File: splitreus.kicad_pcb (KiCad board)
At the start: 2 copper layers, 132.5 x 101 mm, 71 parts, among them J1 TRRS, SW0 SW_PUSH, SW1 SW_PUSH, SW10 SW_PUSH, SW11 SW_PUSH, SW12 SW_PUSH, SW13 SW_PUSH, SW14 SW_PUSH, SW15 SW_PUSH, SW16 SW_PUSH, SW17 SW_PUSH, SW18 SW_PUSH, SW19 SW_PUSH, SW2 SW_PUSH, SW20 SW_PUSH, SW21 SW_PUSH, SW22 SW_PUSH, SW23 SW_PUSH, SW24 SW_PUSH, SW25 SW_PUSH, SW26 SW_PUSH, SW27 SW_PUSH, SW28 SW_PUSH, SW29 SW_PUSH, SW3 SW_PUSH, SW30 SW_PUSH, SW4 SW_PUSH, SW5 SW_PUSH, SW6 SW_PUSH, SW7 SW_PUSH, SW8 SW_PUSH, SW9 SW_PUSH, U1 ProMicro

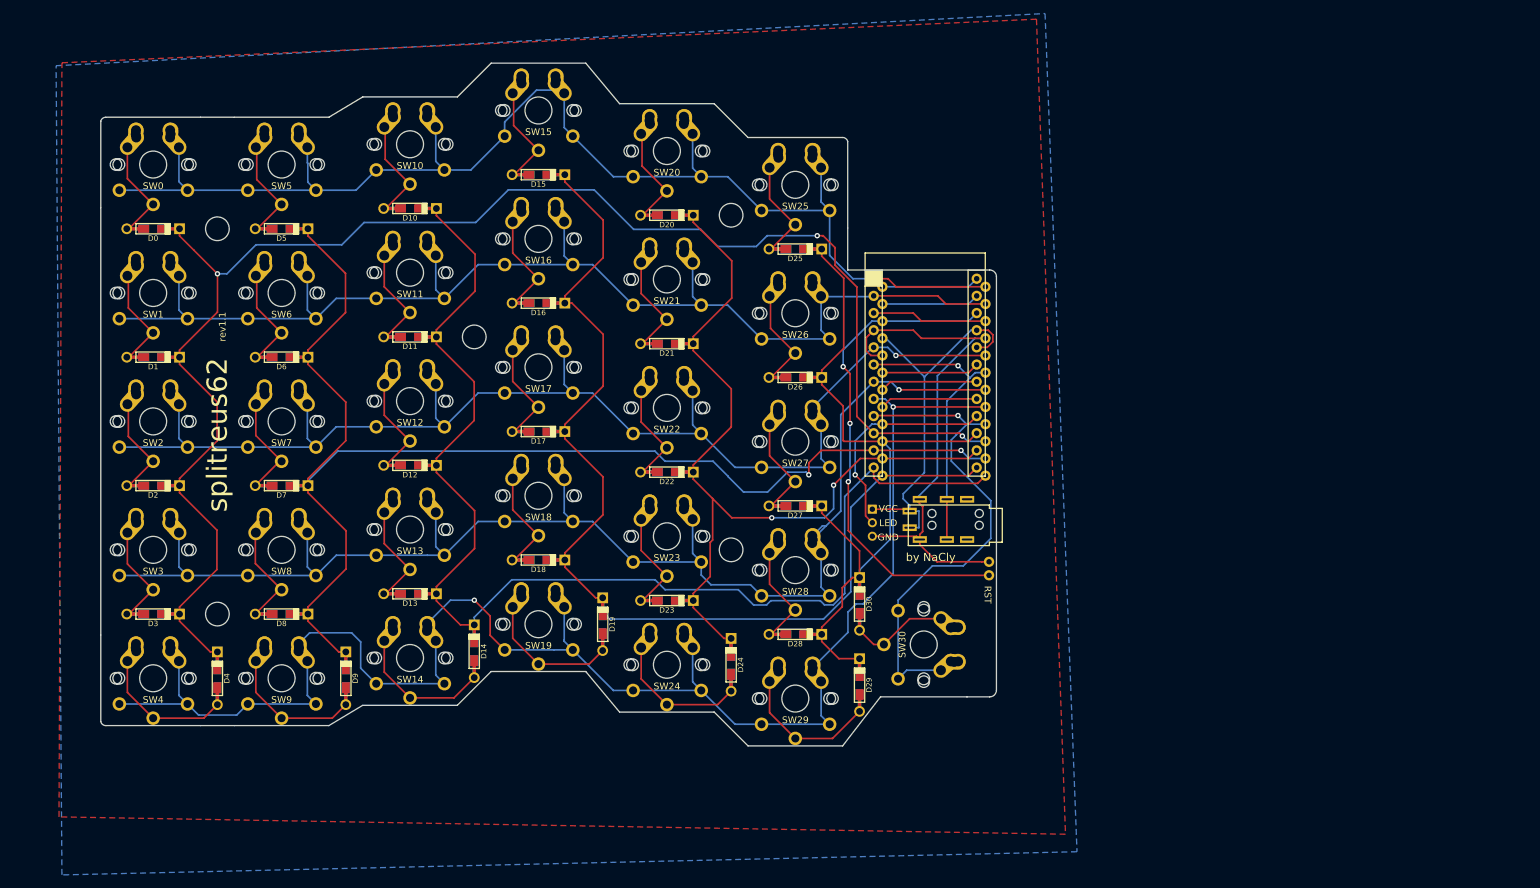
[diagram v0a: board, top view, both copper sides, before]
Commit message: Created kailh_hot_swap
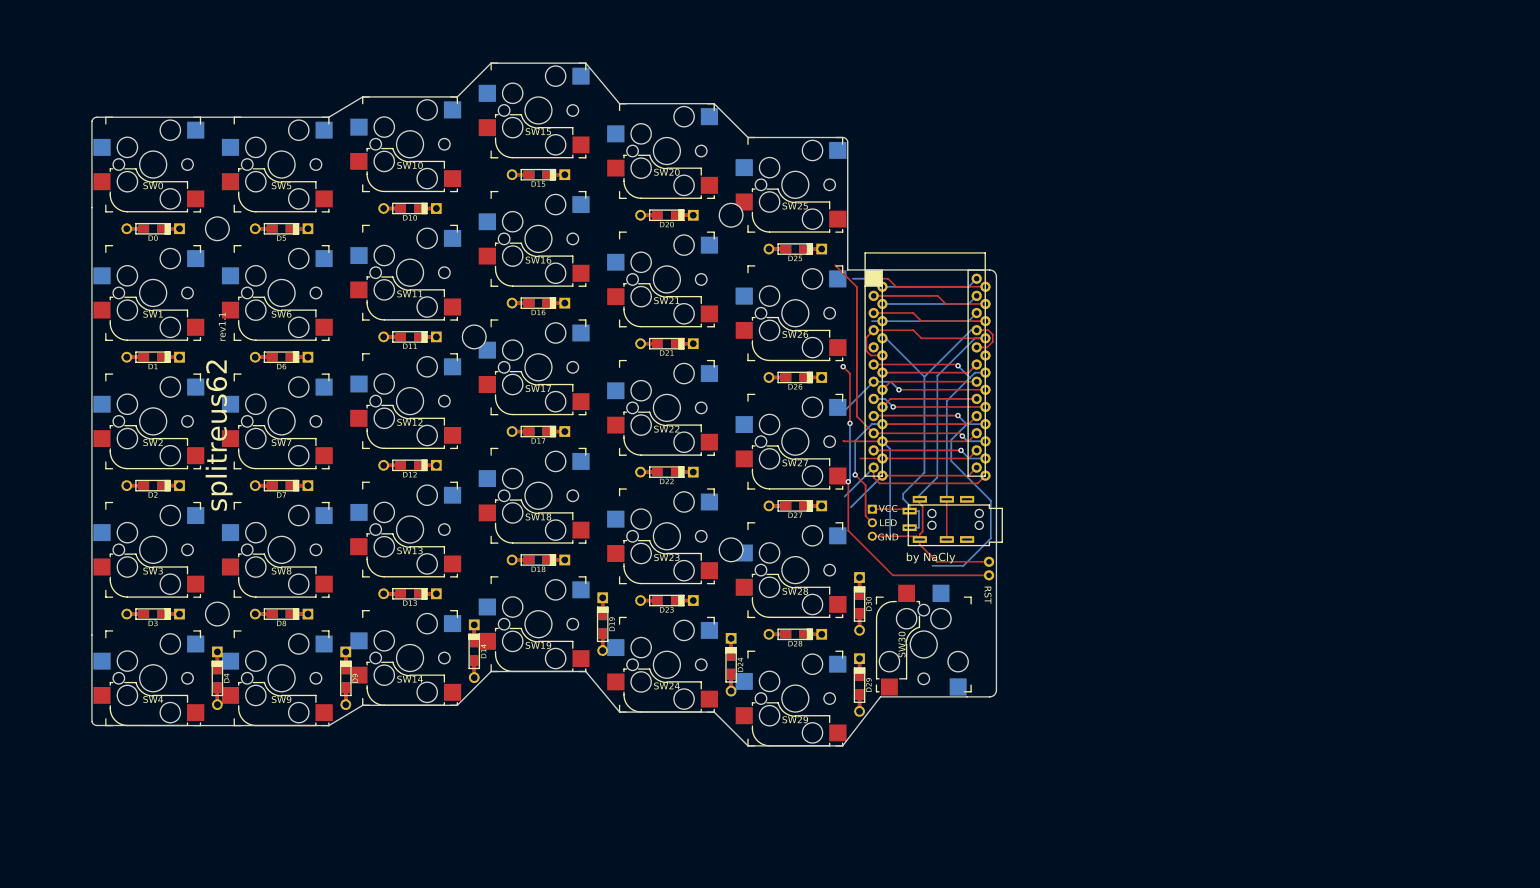
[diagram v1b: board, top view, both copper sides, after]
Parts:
- SW0, SW1, SW10, SW11, SW12, SW13, SW14, SW15, SW16, SW17, SW18, SW19, SW2, SW20, SW21, SW22, SW23, SW24, SW25, SW26, SW27, SW28, SW29, SW3, SW30, SW4, SW5, SW6, SW7, SW8, SW9: footprint Custom Footies:MX-Alps-Choc-1U-No-reversible-fixed -> daprice_kail_mx:Kailh_socket_MX_reversible
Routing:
- net ROW4: track 255.4 -> 17.0 mm, vias 2 -> 1
- net ROW2: track 206.6 -> 0.00 mm, vias 1 -> 0
- net ROW3: track 224.1 -> 23.9 mm
- net COL0: track 240.1 -> 44.3 mm, vias 3 -> 1
- net ROW0: track 209.9 -> 20.1 mm
- net COL1: track 201.9 -> 17.0 mm, vias 2 -> 1
- net ROW1: track 201.7 -> 17.2 mm
- net COL2: track 191.9 -> 24.9 mm
- net COL3: track 165.1 -> 21.1 mm
- net COL4: track 136.2 -> 17.7 mm, vias 2 -> 0
- net COL5: track 122.1 -> 37.8 mm
- net Net-(D29-Pad1): track 26.8 -> 0.00 mm
- net Net-(D14-Pad1): track 26.4 -> 0.00 mm
- net Net-(D9-Pad1): track 26.0 -> 0.00 mm
- net Net-(D4-Pad1): track 26.0 -> 0.00 mm
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- removed copper zone on B.Cu, net (none)
- removed copper zone on F.Cu, net (none)
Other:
- board size 132.5 x 101 mm -> 133.8 x 101 mm

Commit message: updated files
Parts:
- removed REF** (x4): MountingHole_3.5mm, MountingHole:MountingHole_3.5mm
- RST1: footprint Connector_PinHeader_1.27mm:PinHeader_1x02_P1.27mm_Vertical -> Lily58-footprint:TACT_SWITCH_TVBP06
- moved RST1 1.14 mm to (122.6, 61.2), turned to 90 degrees
- renumbered REF** to HOLE4
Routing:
- net RST: track 64.3 -> 14.4 mm, vias 3 -> 0
- net ROW5: track 47.7 -> 17.1 mm
- net COL0: track 44.3 -> 17.0 mm
- net ROW3: track 23.9 -> 17.0 mm
- net COL3: track 21.1 -> 14.4 mm
- net COL2: track 24.9 -> 18.8 mm
- net COL5: track 37.8 -> 31.9 mm
- net COL4: track 17.7 -> 14.4 mm
- net ROW0: track 20.1 -> 17.0 mm
- net GND: track 78.6 -> 76.8 mm

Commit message: Update
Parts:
- removed HOLE4: MountingHole_3.5mm, MountingHole:MountingHole_3.5mm
- moved RST1 8.44 mm to (114.6, 58.7), turned to 0 degrees
- moved D19 0.65 mm to (65.8, 68.0)
- moved D24 0.65 mm to (84.8, 74.0)
- moved D4 0.65 mm to (8.85, 76.0)
- moved D14 0.65 mm to (46.9, 72.0)
- moved D9 0.65 mm to (27.9, 76.0)
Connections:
- U1 pad 20: VCC -> GND
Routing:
- net ROW4: track 17.0 -> 314.6 mm, vias 1 -> 2
- net ROW1: track 17.2 -> 297.6 mm, vias 0 -> 1
- net ROW3: track 17.0 -> 280.4 mm, vias 1 -> 4
- net ROW2: track 0.00 -> 246.4 mm, vias 0 -> 3
- net ROW0: track 17.0 -> 256.8 mm, vias 0 -> 2
- net COL0: track 17.0 -> 239.3 mm
- net COL1: track 17.0 -> 221.3 mm
- net COL2: track 18.8 -> 194.5 mm
- net COL3: track 14.4 -> 171.3 mm, vias 0 -> 1
- net COL4: track 14.4 -> 140.0 mm, vias 0 -> 1
- net COL5: track 31.9 -> 131.2 mm
- net ROW5: track 17.1 -> 81.6 mm
- net RST: track 14.4 -> 62.0 mm
- net Net-(D15-Pad1): track 0.00 -> 46.4 mm
- net Net-(D6-Pad1): track 0.00 -> 39.6 mm
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- added copper zone on B.Cu, net (none)
- added copper zone on F.Cu, net (none)
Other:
- board text added: "rev2.0"
- board text removed: "rev1.1"

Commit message: Update
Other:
- board text removed: "RST"
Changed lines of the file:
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@@
   (general
     (thickness 1.6)
-    (drawings 456)
+    (drawings 454)
     (tracks 1298)
     (zones 0)
@@
   )
   (layers
-    (0 F.Cu signal)
-    (31 B.Cu signal)
+    (0 F.Cu signal hide)
+    (31 B.Cu signal hide)
     (32 B.Adhes user)
     (33 F.Adhes user hide)
@@
       (drillshape 0)
       (scaleselection 1)
-      (outputdirectory "gerber/"))
+      (outputdirectory "C:/Users/Derek/Documents/gerber/sp62_hot/"))
   )
   (net 0 "")
@@
     )
   )
-  (gr_text RST (at 123.4608 63.6372 270) (layer B.SilkS)
-    (effects (font (size 1 1) (thickness 0.2)) (justify mirror))
-  )
-  (gr_text RST (at 123.4608 63.6372 270) (layer F.SilkS)
-    (effects (font (size 1 1) (thickness 0.2)))
-  )
   (gr_text "by NaCly" (at 123.6386 60.7924 270) (layer F.SilkS)
     (effects (font (size 1.2 1.2) (thickness 0.2)))
@@
   (segment (start 105.503 27.5718) (end 105.503 25.597) (width 0.25) (layer F.Cu) (net 40))
   (segment (start 105.503 25.597) (end 106.59 24.51) (width 0.25) (layer F.Cu) (net 40))
+  (segment (start 108.0165 28.1181) (end 108.0164 28.1181) (width 0.25) (layer B.Cu) (net 40))
+  (segment (start 108.0164 28.1181) (end 107.8888 28.2457) (width 0.25) (layer B.Cu) (net 40))
+  (segment (start 108.0165 28.1181) (end 107.889 28.2457) (width 0.25) (layer B.Cu) (net 40))
   (segment (start 84.85 70.1) (end 83.7247 70.1) (width 0.25) (layer F.Cu) (net 41))
   (segment (start 79.9 64.5) (end 79.9 65.6253) (width 0.25) (layer F.Cu) (net 41))
@@
   (segment (start 107.889 20.6257) (end 120.634 20.6257) (width 0.25) (layer B.Cu) (net 45))
   (segment (start 120.634 20.6257) (end 121.83 19.43) (width 0.25) (layer B.Cu) (net 45))
-  (segment (start 108.0165 28.1181) (end 108.0164 28.1181) (width 0.25) (layer B.Cu) (net 40))
-  (segment (start 108.0164 28.1181) (end 107.8888 28.2457) (width 0.25) (layer B.Cu) (net 40))
-  (segment (start 108.0165 28.1181) (end 107.889 28.2457) (width 0.25) (layer B.Cu) (net 40))
   (segment (start 107.889 25.7057) (end 107.8888 25.7057) (width 0.25) (layer B.Cu) (net 46))
   (segment (start 108.144 25.7057) (end 107.889 25.7057) (width 0.25) (layer B.Cu) (net 46))

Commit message: a lot
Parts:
- removed VCC: PinHeader_1x03_P2.00mm_Vertical, Connector_PinHeader_2.00mm:PinHeader_1x03_P2.00mm_Vertical
- D0, D1, D10, D11, D12, D13, D14, D15, D16, D17, D18, D19, D2, D20, D21, D22, D23, D24, D25, D26, D27, D28, D29, D3, D30, D4, D5, D6, D7, D8, D9: value DIODE_SCHOTTKY_SOT23 -> 1N4148; footprint keebio:Diode-Hybrid-reversible -> Custom Footies:Diode-Hybrid-reversible
- U1: footprint Lily58-footprint:ProMicro_rev2 -> Custom Footies:nice_nano
- moved RST1 23.7 mm to (138.2, 59.9)
- moved U1 0.47 mm to (115.4, 32.1), turned to 270 degrees
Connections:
- U1 pad 1: ROW0 -> SERIAL
- U1 pad 10: COL0 -> ROW4
- U1 pad 11: COL1 -> ROW5
- U1 pad 12: COL2 -> COL0
- U1 pad 13: COL3 -> COL1
- U1 pad 14: COL4 -> COL2
- U1 pad 15: COL5 -> COL3
- U1 pad 16: LED -> COL4
- U1 pad 17: Net-(U1-Pad17) -> COL5
- U1 pad 18: Net-(U1-Pad18) -> (no net)
- U1 pad 19: Net-(U1-Pad19) -> (no net)
- U1 pad 2: ROW1 -> ROW0
- U1 pad 20: GND -> VCC
- U1 pad 23: Net-(U1-Pad23) -> GND
- U1 pad 24: Net-(U1-Pad24) -> (no net)
- U1 pad 3: Net-(U1-Pad3) -> GND
- U1 pad 5: ROW2 -> (no net)
- U1 pad 6: SERIAL -> (no net)
- U1 pad 7: ROW3 -> ROW1
- U1 pad 8: ROW4 -> ROW2
- U1 pad 9: ROW5 -> ROW3
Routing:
- net ROW4: track 314.6 -> 0.00 mm, vias 2 -> 0
- net ROW1: track 297.6 -> 0.00 mm, vias 1 -> 0
- net ROW3: track 280.4 -> 0.00 mm, vias 4 -> 0
- net ROW0: track 256.8 -> 0.00 mm, vias 2 -> 0
- net ROW2: track 246.4 -> 0.00 mm, vias 3 -> 0
- net COL0: track 239.3 -> 0.00 mm, vias 1 -> 0
- net COL1: track 221.3 -> 0.00 mm, vias 1 -> 0
- net COL2: track 194.5 -> 0.00 mm
- net COL3: track 171.3 -> 0.00 mm, vias 1 -> 0
- net COL4: track 140.0 -> 0.00 mm, vias 1 -> 0
- net COL5: track 131.2 -> 0.00 mm
- net ROW5: track 81.6 -> 0.00 mm, vias 1 -> 0
- net GND: track 73.4 -> 0.00 mm
- net RST: track 62.0 -> 0.00 mm
- net VCC: track 58.0 -> 0.00 mm
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- removed copper zone on B.Cu, net (none)
- removed copper zone on F.Cu, net (none)
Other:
- board size 133.8 x 101 mm -> 134.3 x 107.2 mm
- board text removed: "by NaCly"
- board text removed: "rev2.0"
- board text removed: "splitreus62"

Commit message: traces
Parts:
- added J2: battery, Connector_PinSocket_2.54mm:PinSocket_1x02_P2.54mm_Vertical, F.Cu at (116.3, 16.0)
- SW0, SW1, SW10, SW11, SW12, SW13, SW14, SW15, SW16, SW17, SW18, SW19, SW2, SW20, SW21, SW22, SW23, SW24, SW25, SW26, SW27, SW28, SW29, SW3, SW30, SW4, SW5, SW6, SW7, SW8, SW9: footprint daprice_kail_mx:Kailh_socket_MX_reversible -> Custom Footies:Kailh_socket_MX_reversible_fix
- moved D29 13.6 mm to (95.2, 87.0), turned to 0 degrees
- moved D14 12.6 mm to (38.1, 81.0), turned to 0 degrees
- moved D4 11.9 mm to (0.00, 84.0), turned to 0 degrees
- moved D9 11.9 mm to (19.1, 84.0), turned to 0 degrees
- moved D19 11.8 mm to (57.1, 76.0), turned to 0 degrees
- moved D24 11.8 mm to (76.2, 82.0), turned to 0 degrees
- moved D30 5.19 mm to (105.9, 70.0), turned to 270 degrees
- moved SW29 0.32 mm to (95.2, 79.2)
- moved SW28 0.29 mm to (95.2, 60.1)
- moved SW24 0.28 mm to (76.2, 74.2)
- moved SW27 0.27 mm to (95.2, 41.1)
- moved SW26 0.25 mm to (95.2, 22.1)
- moved SW19 0.25 mm to (57.1, 68.2)
- moved SW23 0.25 mm to (76.2, 55.1)
- moved D25 0.25 mm to (95.2, 12.5)
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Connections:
- U1 pad 10: ROW4 -> COL2
- U1 pad 11: ROW5 -> ROW2
- U1 pad 12: COL0 -> COL3
- U1 pad 13: COL1 -> ROW3
- U1 pad 14: COL2 -> COL4
- U1 pad 15: COL3 -> ROW4
- U1 pad 16: COL4 -> COL5
- U1 pad 17: COL5 -> ROW5
- U1 pad 2: ROW0 -> COL0
- U1 pad 7: ROW1 -> ROW0
- U1 pad 8: ROW2 -> COL1
- U1 pad 9: ROW3 -> ROW1
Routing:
- net COL0: track 0.00 -> 252.0 mm
- net COL1: track 0.00 -> 210.4 mm, vias 0 -> 2
- net ROW4: track 0.00 -> 173.0 mm, vias 0 -> 7
- net COL2: track 0.00 -> 172.3 mm, vias 0 -> 2
- net ROW0: track 0.00 -> 165.7 mm, vias 0 -> 6
- net ROW3: track 0.00 -> 165.7 mm, vias 0 -> 6
- net COL4: track 0.00 -> 155.1 mm, vias 0 -> 2
- net ROW1: track 0.00 -> 149.9 mm, vias 0 -> 6
- net COL3: track 0.00 -> 148.5 mm, vias 0 -> 2
- net ROW2: track 0.00 -> 130.9 mm, vias 0 -> 6
- net COL5: track 0.00 -> 125.3 mm, vias 0 -> 1
- net ROW5: track 0.00 -> 62.6 mm, vias 0 -> 2
- net GND: track 0.00 -> 50.8 mm
- net SERIAL: track 0.00 -> 42.0 mm
- net VCC: track 0.00 -> 37.0 mm, vias 0 -> 1
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
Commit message: traces routed
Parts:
- moved RST1 42.1 mm to (118.7, 22.7), turned to 90 degrees
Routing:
- net RST: track 0.00 -> 5.70 mm
- net GND: track 50.8 -> 52.1 mm

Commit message: leds
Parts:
- added D90: SK6812MINI, Custom Footies:sk6812_minie_reversible, F.Cu at (163.5, 30.8)
- added D91: SK6812MINI, Custom Footies:sk6812_minie_reversible, F.Cu at (156.4, 15.6)
- added D910: SK6812MINI, Custom Footies:sk6812_minie_reversible, F.Cu at (156.4, 30.8)
- added D911: SK6812MINI, Custom Footies:sk6812_minie_reversible, F.Cu at (163.5, 25.7)
- added D912: SK6812MINI, Custom Footies:sk6812_minie_reversible, F.Cu at (170.5, 20.7)
- added D913: SK6812MINI, Custom Footies:sk6812_minie_reversible, F.Cu at (177.5, 15.6)
- added D914: SK6812MINI, Custom Footies:sk6812_minie_reversible, F.Cu at (184.5, 10.6)
- added D915: SK6812MINI, Custom Footies:sk6812_minie_reversible, F.Cu at (170.5, 25.7)
- added D916: SK6812MINI, Custom Footies:sk6812_minie_reversible, F.Cu at (154.7, 5.84)
- added D917: SK6812MINI, Custom Footies:sk6812_minie_reversible, F.Cu at (177.5, 20.7)
- added D918: SK6812MINI, Custom Footies:sk6812_minie_reversible, F.Cu at (184.5, 15.6)
- added D919: SK6812MINI, Custom Footies:sk6812_minie_reversible, F.Cu at (191.5, 10.6)
- added D92: SK6812MINI, Custom Footies:sk6812_minie_reversible, F.Cu at (163.5, 10.6)
- added D920: SK6812MINI, Custom Footies:sk6812_minie_reversible, F.Cu at (170.5, 30.8)
- added D921: SK6812MINI, Custom Footies:sk6812_minie_reversible, F.Cu at (177.5, 25.7)
- added D922: SK6812MINI, Custom Footies:sk6812_minie_reversible, F.Cu at (184.5, 20.7)
- added D923: SK6812MINI, Custom Footies:sk6812_minie_reversible, F.Cu at (191.5, 15.6)
- added D924: SK6812MINI, Custom Footies:sk6812_minie_reversible, F.Cu at (198.6, 10.6)
- added D925: SK6812MINI, Custom Footies:sk6812_minie_reversible, F.Cu at (177.5, 30.8)
- added D926: SK6812MINI, Custom Footies:sk6812_minie_reversible, F.Cu at (184.5, 25.7)
- added D927: SK6812MINI, Custom Footies:sk6812_minie_reversible, F.Cu at (191.5, 20.7)
- added D928: SK6812MINI, Custom Footies:sk6812_minie_reversible, F.Cu at (198.6, 15.6)
- added D929: SK6812MINI, Custom Footies:sk6812_minie_reversible, F.Cu at (184.5, 30.8)
- added D93: SK6812MINI, Custom Footies:sk6812_minie_reversible, F.Cu at (156.4, 20.7)
- added D930: SK6812MINI, Custom Footies:sk6812_minie_reversible, F.Cu at (191.5, 25.7)
- added D94: SK6812MINI, Custom Footies:sk6812_minie_reversible, F.Cu at (163.5, 15.6)
- added D95: SK6812MINI, Custom Footies:sk6812_minie_reversible, F.Cu at (170.5, 10.6)
- added D96: SK6812MINI, Custom Footies:sk6812_minie_reversible, F.Cu at (156.4, 25.7)
- added D97: SK6812MINI, Custom Footies:sk6812_minie_reversible, F.Cu at (163.5, 20.7)
- added D98: SK6812MINI, Custom Footies:sk6812_minie_reversible, F.Cu at (170.5, 15.6)
- added D99: SK6812MINI, Custom Footies:sk6812_minie_reversible, F.Cu at (177.5, 10.6)
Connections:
- J1 pad 1: Net-(J1-Pad1) -> to_right
- U1 pad 18: (no net) -> LED
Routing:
- net to_right: track 0.00 -> 5.95 mm
- net Net-(J1-Pad1): track 5.95 -> 0.00 mm
